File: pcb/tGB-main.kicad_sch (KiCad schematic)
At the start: 69 parts, among them J1 DMG-CardEdge, J2 PROG_PORT, Q1 DMG3415U, Q2 HN4A56JU, Q3 2N7002K, U1 TC74LCXR163245FT, U2 TC74LCXR163245FT, U3 ICE40UP5K-SG48ITR, U4 TPS79901DDCR, U5 TPS79901DDCR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

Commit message: rename project
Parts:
- J1: value DMG-CardEdge -> GB-CardEdge; footprint DMG-CardEdge:DMG-CardEdge -> GB-CardEdge:GB-CardEdge; symbol DMG-CardEdge:DMG-CardEdge -> GB-CardEdge:GB-CardEdge
- J2: footprint pinheader:pinheader-10p-sm -> PinHeader:PinHeader-10P-Sidemount
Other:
- note added: "20kHz -40dB/dec LPF for external audio input"
- note added: "600Ω"
- note added: "Reset request from cartridge to system"
- note added: "Reverse current protection"
- note removed: "20kHz -40dB/dec LPF for audio input(VIN)"
- title: (none) -> tsuraraGB main board
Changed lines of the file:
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@@
   (paper "A3")
   (title_block
+    (title "tsuraraGB main board")
     (rev "B")
   )
@@
     (effects (font (size 1.27 1.27)) (justify right bottom))
   )
+  (text "600Ω" (at 357.505 229.235 0)
+    (effects (font (size 1.27 1.27)) (justify left bottom))
+  )
   (text "YELLOW" (at 254 149.86 0)
     (effects (font (size 1.27 1.27)) (justify left bottom))
@@
     (effects (font (size 1.27 1.27)) (justify right bottom))
   )
+  (text "Reverse current protection" (at 41.91 22.86 0)
+    (effects (font (size 1.27 1.27)) (justify left bottom))
+  )
+  (text "Reset request from cartridge to system" (at 240.03 223.52 0)
+    (effects (font (size 1.27 1.27) italic) (justify left bottom))
+  )
   (text "BLUE" (at 237.49 102.87 180)
     (effects (font (size 1.27 1.27)) (justify right bottom))
   )
-  (text "20kHz -40dB/dec LPF for audio input(VIN)" (at 238.76 262.89 0)
+  (text "600Ω" (at 380.365 192.405 0)
+    (effects (font (size 1.27 1.27)) (justify left bottom))
+  )
+  (text "20kHz -40dB/dec LPF for external audio input" (at 237.49 262.89 0)
     (effects (font (size 1.27 1.27) italic) (justify left bottom))
   )
@@
     (pin "1")
   )
-  (symbol (lib_id "DMG-CardEdge:DMG-CardEdge") (at 34.29 149.86 0) (unit 1)
+  (symbol (lib_id "GB-CardEdge:GB-CardEdge") (at 34.29 149.86 0) (unit 1)
     (in_bom yes) (on_board yes)
     (property "Reference" "J1" (id 0) (at 35.7632 98.679 0))
-    (property "Value" "DMG-CardEdge" (id 1) (at 35.7632 100.9904 0))
-    (property "Footprint" "DMG-CardEdge:DMG-CardEdge" (id 2) (at 34.29 198.12 0)
+    (property "Value" "GB-CardEdge" (id 1) (at 35.7632 100.9904 0))
+    (property "Footprint" "GB-CardEdge:GB-CardEdge" (id 2) (at 34.29 198.12 0)
       (effects (font (size 1.27 1.27)) hide)
     )
@@
     (property "Reference" "J2" (id 0) (at 295.91 49.53 0))
     (property "Value" "PROG_PORT" (id 1) (at 295.91 80.01 0))
-    (property "Footprint" "pinheader:pinheader-10p-sm" (id 2) (at 295.91 63.5 0)
+    (property "Footprint" "PinHeader:PinHeader-10P-Sidemount" (id 2) (at 295.91 63.5 0)
       (effects (font (size 1.27 1.27)) hide)
     )
@@
     )
     (path "/00000000-0000-0000-0000-00005fc7ddc7"
-      (reference "J1") (unit 1) (value "DMG-CardEdge") (footprint "DMG-CardEdge:DMG-CardEdge")
+      (reference "J1") (unit 1) (value "GB-CardEdge") (footprint "GB-CardEdge:GB-CardEdge")
     )
     (path "/00000000-0000-0000-0000-00006027ac0d"
-      (reference "J2") (unit 1) (value "PROG_PORT") (footprint "pinheader:pinheader-10p-sm")
+      (reference "J2") (unit 1) (value "PROG_PORT") (footprint "PinHeader:PinHeader-10P-Sidemount")
     )
     (path "/d5f93cc2-b1a6-4187-bb4c-8f284d837e5c"

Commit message: rename project, update pcb
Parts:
- added FB1: MPZ1608S601ATA00, Inductor_SMD:L_0603_1608Metric, symbol Device:FerriteBead
- renumbered FB1 to FB2, FB2 to FB3
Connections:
- net VCC: now also FB1.1; no longer Q1.3 (D), Q2.1 (E1), R2.1
- new net VCC0: FB1.2, Q1.3 (D), Q2.1 (E1), R2.1
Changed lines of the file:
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@@
   (junction (at 102.87 156.21) (diameter 0) (color 0 0 0 0)
   )
-  (junction (at 39.37 41.91) (diameter 0) (color 0 0 0 0)
+  (junction (at 37.465 41.91) (diameter 0) (color 0 0 0 0)
   )
   (junction (at 161.29 171.45) (diameter 0) (color 0 0 0 0)
@@
     (stroke (width 0) (type default) (color 0 0 0 0))
   )
-  (wire (pts (xy 39.37 41.91) (xy 50.8 41.91))
+  (wire (pts (xy 37.465 41.91) (xy 50.8 41.91))
     (stroke (width 0) (type default) (color 0 0 0 0))
   )
@@
     (stroke (width 0) (type default) (color 0 0 0 0))
   )
-  (wire (pts (xy 39.37 93.98) (xy 39.37 41.91))
+  (wire (pts (xy 37.465 93.98) (xy 37.465 67.31))
     (stroke (width 0) (type default) (color 0 0 0 0))
   )
@@
     (stroke (width 0) (type default) (color 0 0 0 0))
   )
-  (wire (pts (xy 39.37 30.48) (xy 39.37 41.91))
+  (wire (pts (xy 37.465 30.48) (xy 37.465 41.91))
     (stroke (width 0) (type default) (color 0 0 0 0))
   )
@@
     (stroke (width 0) (type default) (color 0 0 0 0))
   )
-  (wire (pts (xy 52.07 30.48) (xy 39.37 30.48))
+  (wire (pts (xy 52.07 30.48) (xy 37.465 30.48))
     (stroke (width 0) (type default) (color 0 0 0 0))
   )
@@
     (stroke (width 0) (type default) (color 0 0 0 0))
   )
+  (wire (pts (xy 37.465 59.69) (xy 37.465 41.91))
+    (stroke (width 0) (type default) (color 0 0 0 0))
+  )
   (wire (pts (xy 330.2 45.72) (xy 330.2 44.45))
     (stroke (width 0) (type default) (color 0 0 0 0))
@@
     (stroke (width 0) (type default) (color 0 0 0 0))
   )
-  (wire (pts (xy 53.34 93.98) (xy 39.37 93.98))
+  (wire (pts (xy 53.34 93.98) (xy 37.465 93.98))
     (stroke (width 0) (type default) (color 0 0 0 0))
   )
@@
     (effects (font (size 1.27 1.27)) (justify left bottom))
   )
+  (text "600Ω" (at 29.21 67.945 0)
+    (effects (font (size 1.27 1.27)) (justify left bottom))
+  )
   (text "20kHz -40dB/dec LPF for external audio input" (at 237.49 262.89 0)
     (effects (font (size 1.27 1.27) italic) (justify left bottom))
@@
     (effects (font (size 1.27 1.27)) (justify left bottom))
   )
+  (label "VCC0" (at 37.465 41.91 180)
+    (effects (font (size 1.27 1.27)) (justify right bottom))
+  )
   (label "CB-A10" (at 91.44 74.93 0)
     (effects (font (size 1.27 1.27)) (justify left bottom))
@@
     (pin "1")
   )
+  (symbol (lib_id "Device:FerriteBead") (at 37.465 63.5 180) (unit 1)
+    (in_bom yes) (on_board yes)
+    (property "Reference" "FB1" (id 0) (at 32.385 62.23 0))
+    (property "Value" "MPZ1608S601ATA00" (id 1) (at 24.765 64.77 0))
+    (property "Footprint" "Inductor_SMD:L_0603_1608Metric" (id 2) (at 39.243 63.5 90)
+      (effects (font (size 1.27 1.27)) hide)
+    )
+    (property "Datasheet" "~" (id 3) (at 37.465 63.5 0)
+      (effects (font (size 1.27 1.27)) hide)
+    )
+    (pin "1")
+    (pin "2")
+  )
   (symbol (lib_id "power:GND") (at 254 254 0) (unit 1)
     (in_bom yes) (on_board yes)
@@
   (symbol (lib_id "HN4A56JU:HN4A56JU") (at 55.88 55.88 0) (mirror y) (unit 1)
     (in_bom yes) (on_board yes)
-    (property "Reference" "Q2" (id 0) (at 66.04 54.61 0)
+    (property "Reference" "Q2" (id 0) (at 48.895 55.245 0)
       (effects (font (size 1.27 1.27)) (justify left))
     )
-    (property "Value" "HN4A56JU" (id 1) (at 73.66 57.15 0)
+    (property "Value" "HN4A56JU" (id 1) (at 48.895 57.15 0)
       (effects (font (size 1.27 1.27)) (justify left))
     )
@@
   (symbol (lib_id "Device:FerriteBead") (at 355.6 223.52 90) (unit 1)
     (in_bom yes) (on_board yes)
-    (property "Reference" "FB1" (id 0) (at 355.6 219.71 90))
+    (property "Reference" "FB2" (id 0) (at 355.6 219.71 90))
     (property "Value" "MPZ1608S601ATA00" (id 1) (at 367.03 226.06 90))
     (property "Footprint" "Inductor_SMD:L_0603_1608Metric" (id 2) (at 355.6 225.298 90)
@@
   (symbol (lib_id "Device:FerriteBead") (at 378.46 186.69 90) (unit 1)
     (in_bom yes) (on_board yes)
-    (property "Reference" "FB2" (id 0) (at 378.46 182.88 90))
+    (property "Reference" "FB3" (id 0) (at 378.46 182.88 90))
     (property "Value" "MPZ1608S601ATA00" (id 1) (at 389.89 189.23 90))
     (property "Footprint" "Inductor_SMD:L_0603_1608Metric" (id 2) (at 378.46 188.468 90)
@@
       (reference "D5") (unit 1) (value "BAT43XV2") (footprint "Diode_SMD:D_SOD-523")
     )
-    (path "/7c3d26c3-ca15-403e-b93f-6e0d11b0bbfa"
+    (path "/640fad2a-b060-455a-9d59-aabe52e9ef13"
       (reference "FB1") (unit 1) (value "MPZ1608S601ATA00") (footprint "Inductor_SMD:L_0603_1608Metric")
     )
-    (path "/81c7c679-596c-4fdb-9bd0-fb247b197f32"
+    (path "/7c3d26c3-ca15-403e-b93f-6e0d11b0bbfa"
       (reference "FB2") (unit 1) (value "MPZ1608S601ATA00") (footprint "Inductor_SMD:L_0603_1608Metric")
     )
+    (path "/81c7c679-596c-4fdb-9bd0-fb247b197f32"
+      (reference "FB3") (unit 1) (value "MPZ1608S601ATA00") (footprint "Inductor_SMD:L_0603_1608Metric")
+    )
     (path "/00000000-0000-0000-0000-00005fc7ddc7"

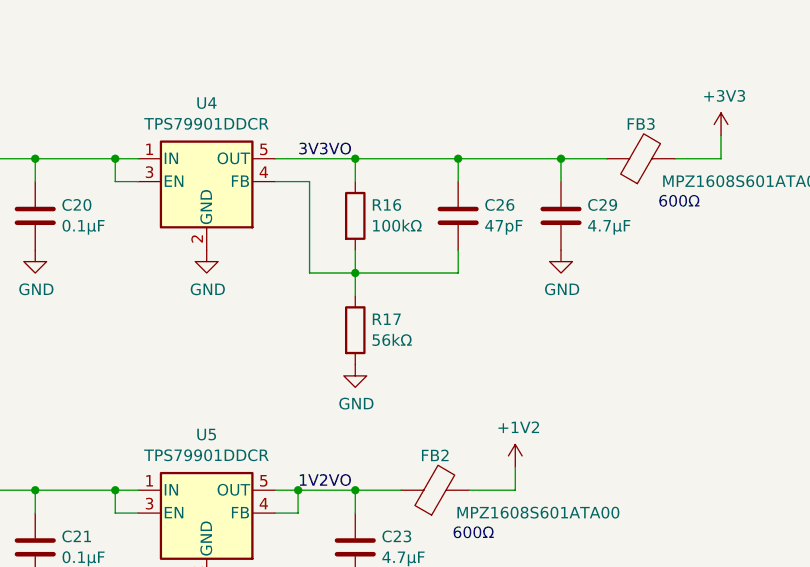
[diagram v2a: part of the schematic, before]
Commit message: update R16,R17 value
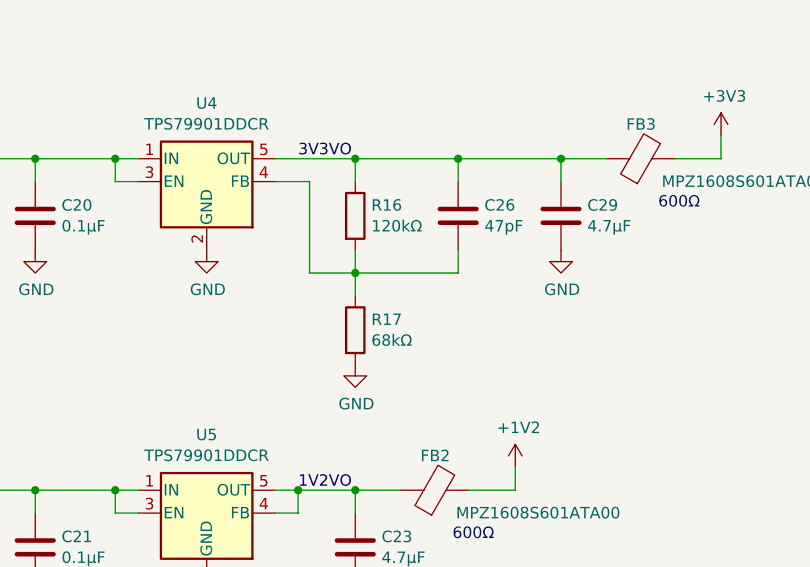
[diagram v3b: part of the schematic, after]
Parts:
- R16: value 100kΩ -> 120kΩ
- R17: value 56kΩ -> 68kΩ
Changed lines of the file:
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@@
       (effects (font (size 1.27 1.27)) (justify left))
     )
-    (property "Value" "100kΩ" (id 1) (at 348.488 194.183 0)
+    (property "Value" "120kΩ" (id 1) (at 348.488 194.183 0)
       (effects (font (size 1.27 1.27)) (justify left))
     )
@@
       (effects (font (size 1.27 1.27)) (justify left))
     )
-    (property "Value" "56kΩ" (id 1) (at 348.488 206.883 0)
+    (property "Value" "68kΩ" (id 1) (at 348.488 206.883 0)
       (effects (font (size 1.27 1.27)) (justify left))
     )
@@
     )
     (path "/00000000-0000-0000-0000-00005fc2fe08"
-      (reference "R16") (unit 1) (value "100kΩ") (footprint "Resistor_SMD:R_0402_1005Metric")
+      (reference "R16") (unit 1) (value "120kΩ") (footprint "Resistor_SMD:R_0402_1005Metric")
     )
     (path "/00000000-0000-0000-0000-00005fc34016"
-      (reference "R17") (unit 1) (value "56kΩ") (footprint "Resistor_SMD:R_0402_1005Metric")
+      (reference "R17") (unit 1) (value "68kΩ") (footprint "Resistor_SMD:R_0402_1005Metric")
     )
     (path "/00000000-0000-0000-0000-000060318ae2"
